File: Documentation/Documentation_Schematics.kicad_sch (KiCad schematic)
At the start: 19 parts

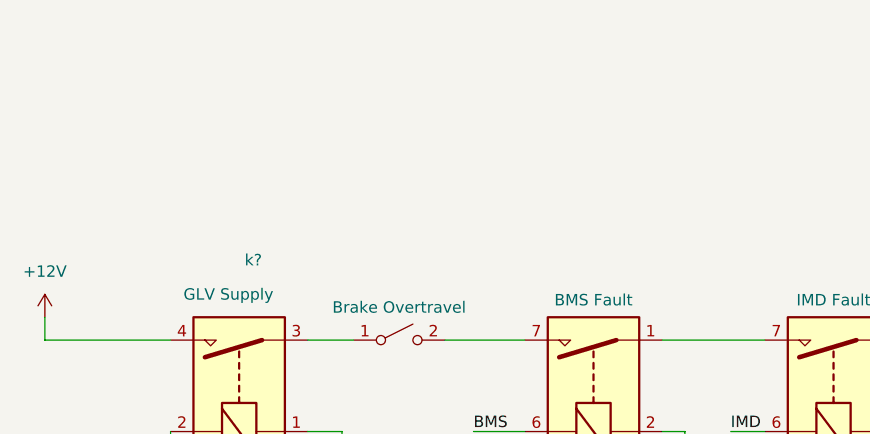
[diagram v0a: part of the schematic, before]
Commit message: added battery
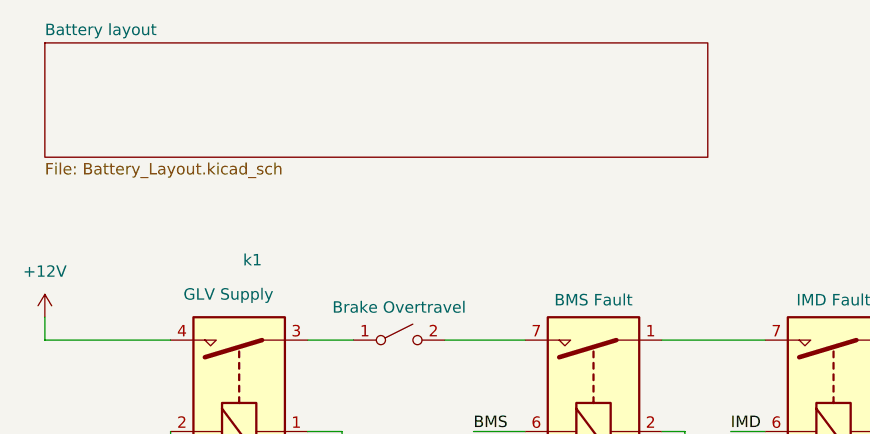
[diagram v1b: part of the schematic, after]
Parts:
- gave numbers to parts that had none: 19
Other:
- added sheet Battery layout (Battery_Layout.kicad_sch)

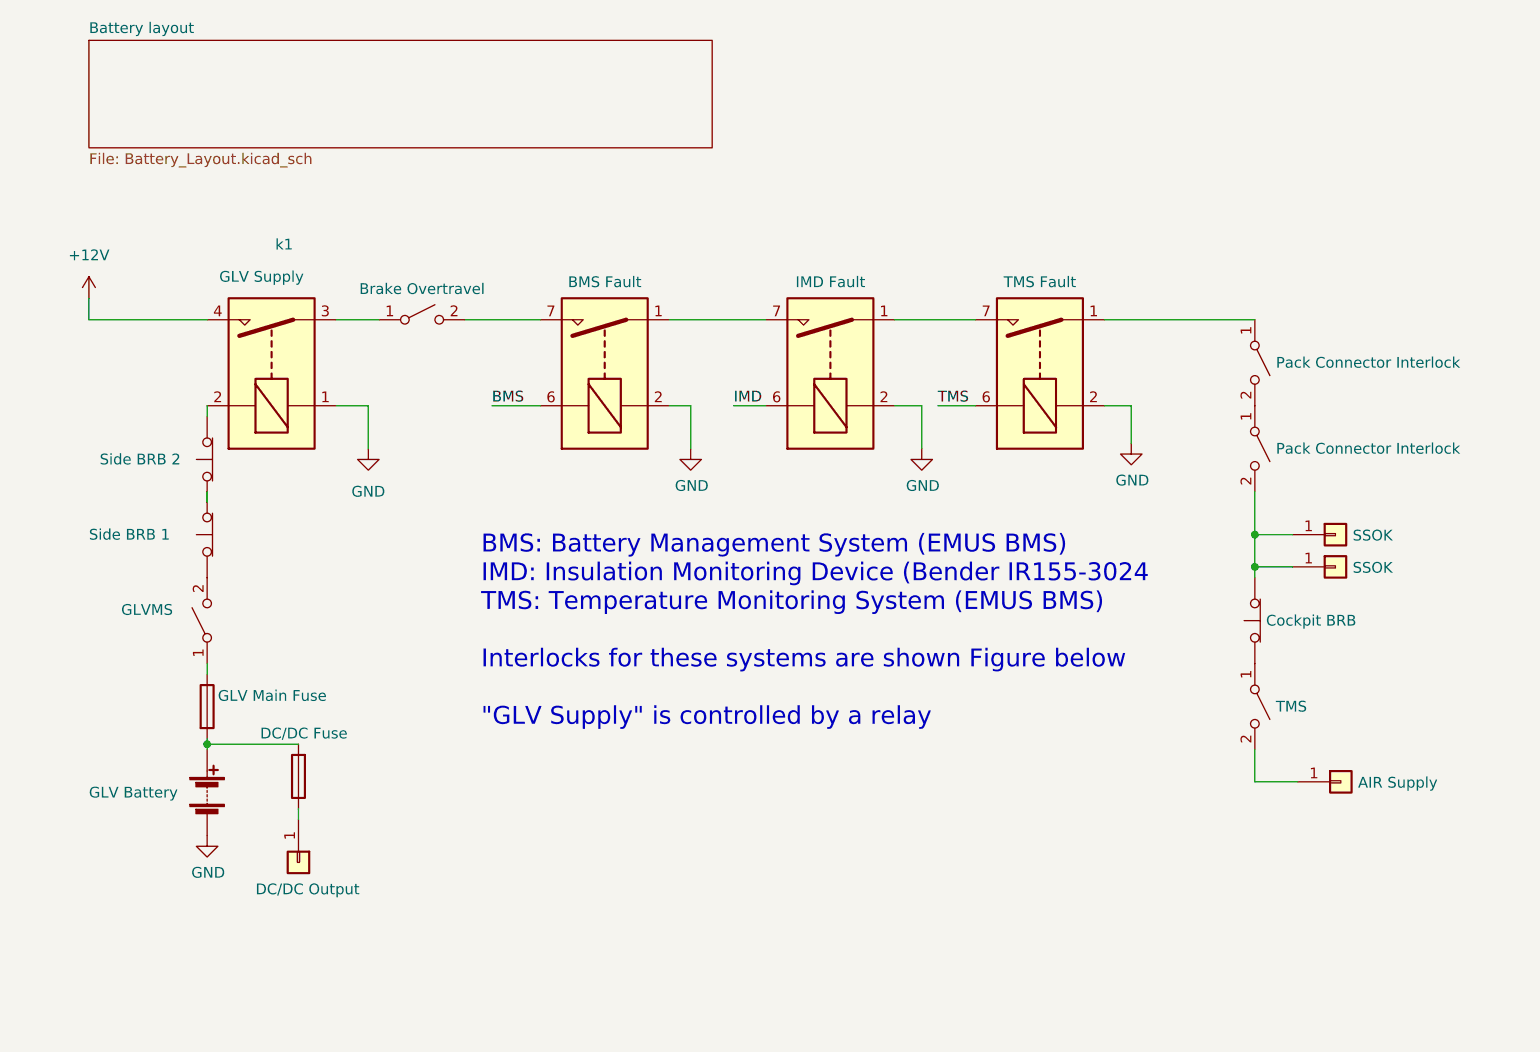
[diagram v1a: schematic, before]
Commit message: finished battery schematic and saftey loop
finished battery schematic and saftey loop
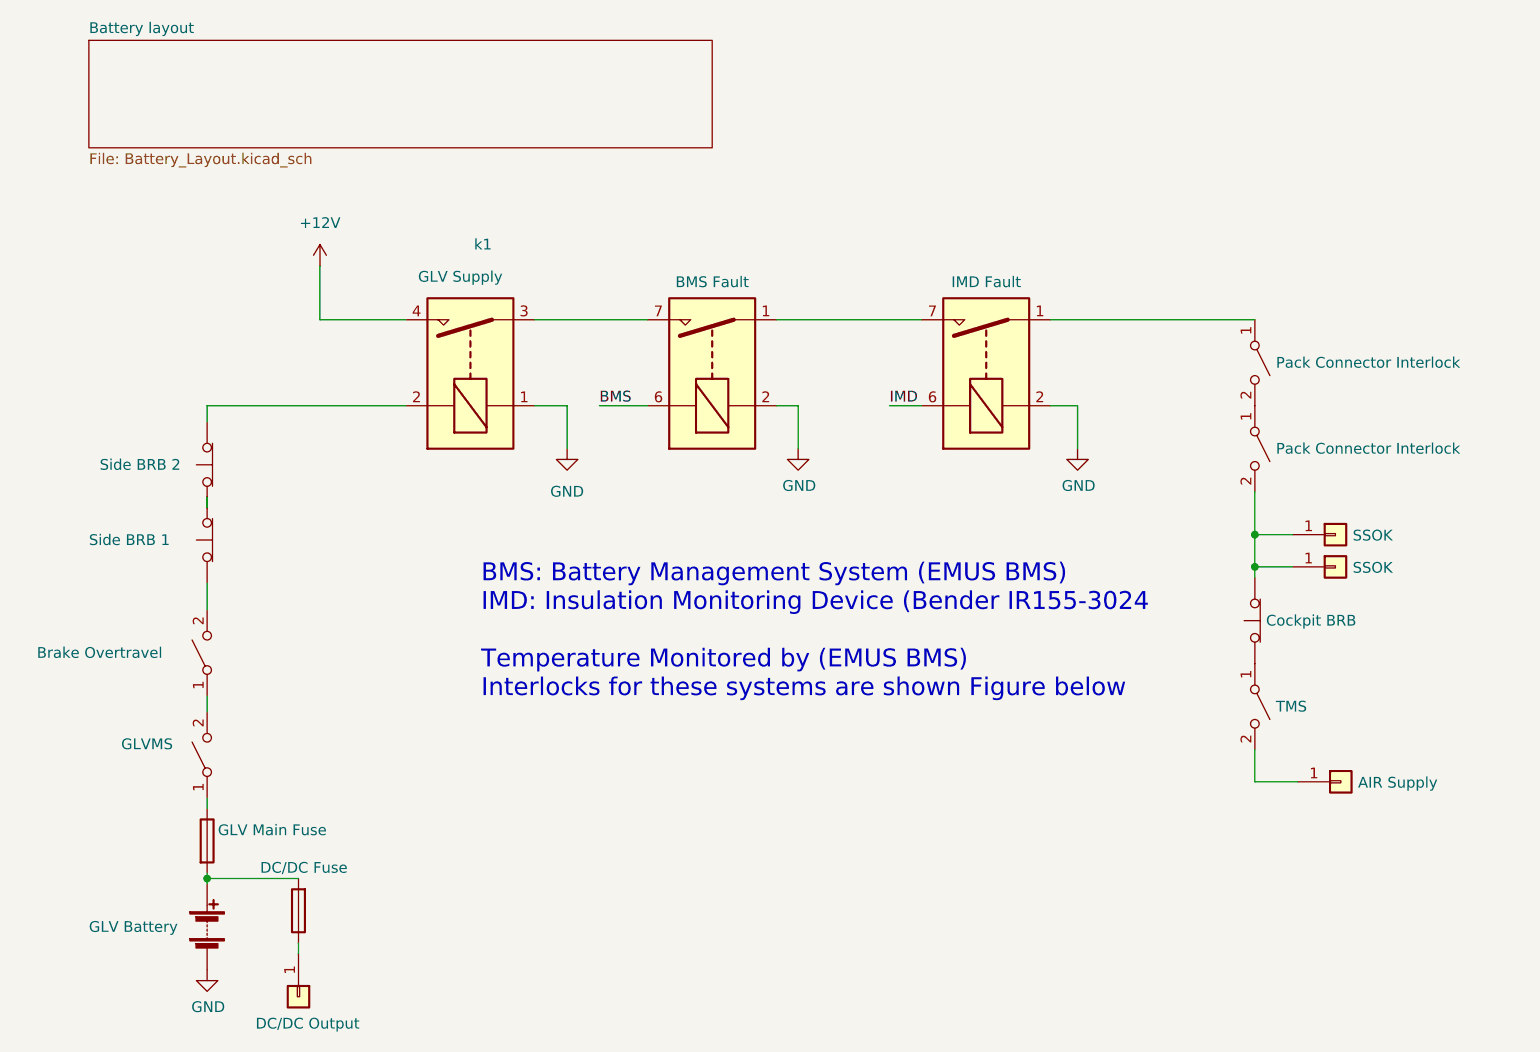
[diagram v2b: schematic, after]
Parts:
- removed K3: TMS Fault, Relay_THT:Relay_StandexMeder_DIP_LowProfile, symbol Relay:DIPxx-1Axx-11x
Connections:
- net at SW3.2 (B): now also SW4.1 (A); no longer SW2.1 (A)
- net at k1.3: now also K1.7, K1.8; no longer SW4.1 (A)
- net at K2.1, K2.14: now also SW5.1 (A)
- new net: SW2.1 (A), SW4.2 (B)
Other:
- note added: "BMS: Battery Management System (EMUS BMS) IMD: Insulation Monitoring Device (Bender IR155-3024 Temperature Monitored by (EMUS BMS) Interlocks for these systems are shown Figure below"
- note removed: "BMS: Battery Management System (EMUS BMS) IMD: Insulation Monitoring Device (Bender IR155-3024 TMS: Temperature Monitoring System (EMUS BMS) Interlocks for these systems are shown Figure below "GLV Supply" is controlled by a relay"
- moved on the sheet: k1
